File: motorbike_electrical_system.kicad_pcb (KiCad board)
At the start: 2 copper layers, 92.4 x 87.5 mm, 94 parts, among them IC1 BDX34C, IC2 BDX34C, IC3 BDX34C, IC4 BDX34C, IC5 BDX34C, IC6 BDX34C, U1 L7805, U2 L7805, U3 L7805

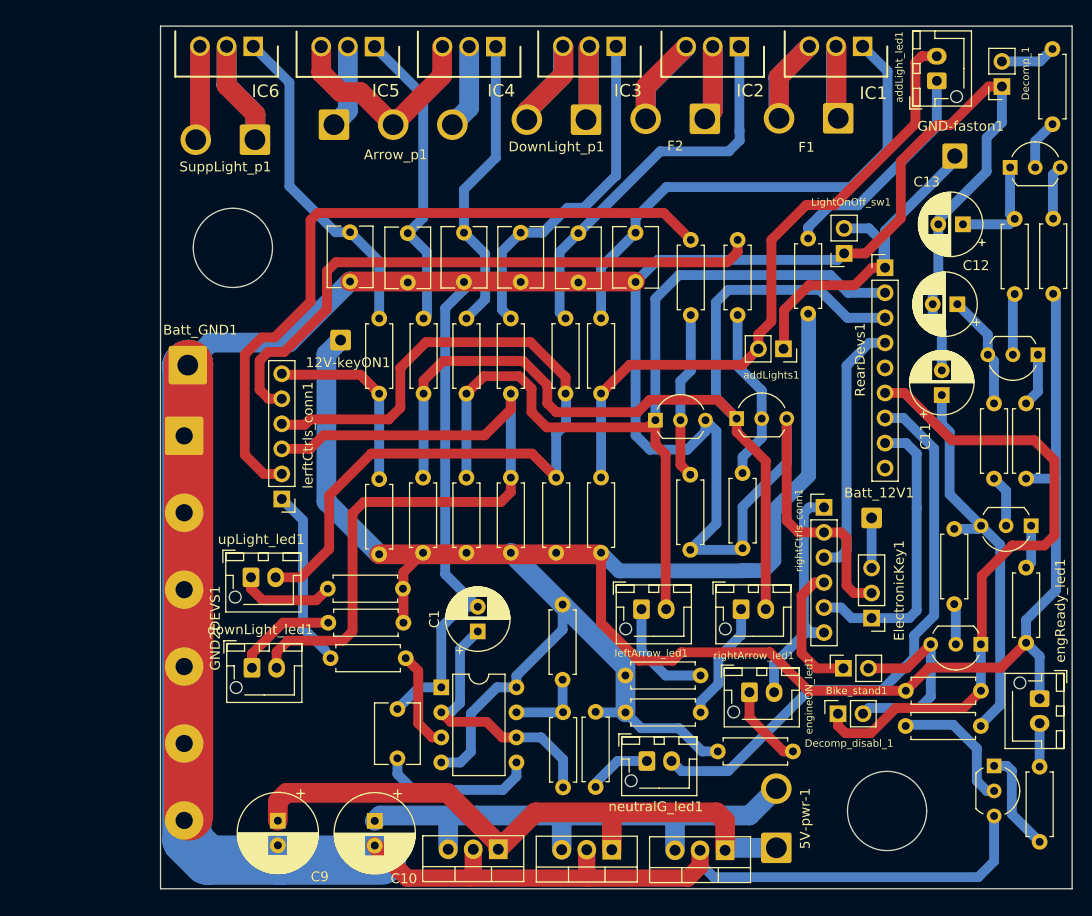
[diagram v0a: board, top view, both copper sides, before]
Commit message: PCB size reduction
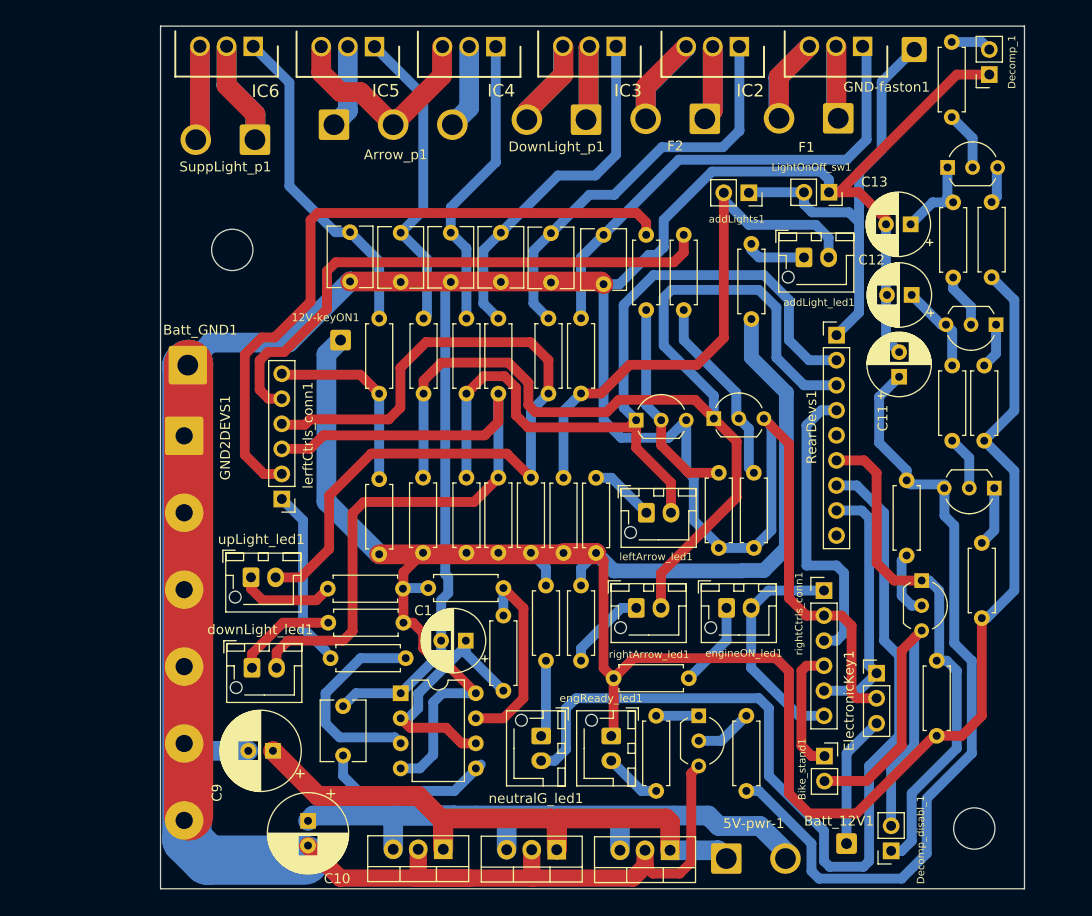
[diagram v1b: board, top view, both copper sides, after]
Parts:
- moved engReady_led1 43.6 mm to (168.9, 122.6)
- moved RA7 39.0 mm to (173.5, 128.2), turned to 90 degrees
- moved Batt_12V1 33.1 mm to (192.8, 133.5)
- moved DC5 30.4 mm to (177.8, 120.5)
- moved RL3 22.7 mm to (167.4, 96.4), turned to -90 degrees
- moved addLight_led1 22.4 mm to (188.5, 74.1), turned to 0 degrees
- moved addLights1 16.2 mm to (182.9, 67.5)
- moved RA5 16.2 mm to (182.6, 120.5), turned to -90 degrees
- moved Decomp_disabl_1 14.9 mm to (197.3, 134.2), turned to 180 degrees
- moved RL5 13.8 mm to (162.3, 115.0)
- moved RL4 13.2 mm to (165.9, 115.0), turned to 90 degrees
- moved RL6 12.9 mm to (176.8, 116.7)
- moved GND-faston1 11.6 mm to (199.7, 53.0)
- moved RC1 11.5 mm to (158.0, 110.4)
- moved RC2 11.1 mm to (158.0, 107.6), turned to 180 degrees
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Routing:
- net Net-(C11-Pad1): track 39.6 -> 81.6 mm
- net Net-(RearDevs1-Pad7): track 58.1 -> 94.6 mm
- net Net-(Bike_stand1-Pad2): track 20.2 -> 42.9 mm
- net GND: track 461.1 -> 440.4 mm
- net Net-(5V-pwr-1-Pad2): track 52.8 -> 72.7 mm
- net Net-(RL7-Pad1): track 23.1 -> 6.26 mm
- net Net-(DC4-Pad1): track 66.2 -> 52.6 mm
- net Net-(RC1-Pad1): track 8.05 -> 20.5 mm
- net Net-(RE1-Pad1): track 10.1 -> 21.4 mm
- net Net-(RBT6-Pad2): track 66.1 -> 55.8 mm
- net Net-(Batt_12V1-Pad1): track 5.08 -> 13.5 mm
- net Net-(Q_arr2-Pad1): track 99.0 -> 107.3 mm
- net Net-(GND-faston1-Pad1): track 37.4 -> 45.4 mm
- net Net-(DC5-Pad2): track 13.7 -> 5.88 mm
- net Net-(Q_arr1-Pad1): track 89.2 -> 82.4 mm
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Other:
- board size 92.4 x 87.5 mm -> 87.6 x 87.5 mm

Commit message: Fix: wrong power transistor orientation (and PCB's size reducing)
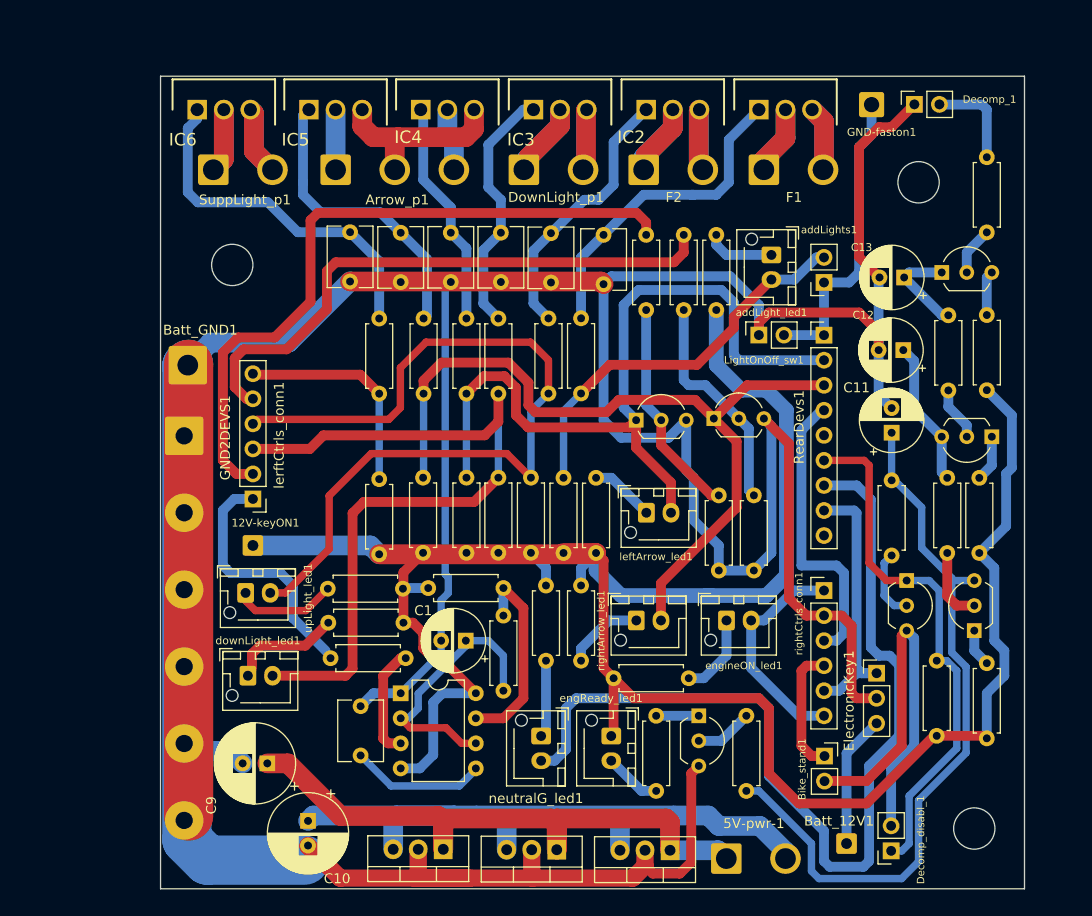
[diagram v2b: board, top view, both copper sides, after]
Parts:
- moved 12V-keyON1 22.6 mm to (132.6, 103.3)
- moved LightOnOff_sw1 16.1 mm to (183.9, 81.9), turned to 90 degrees
- moved DC3 14.6 mm to (205.7, 111.9), turned to 90 degrees
- moved IC1 12.3 mm to (183.9, 59.1), turned to 0 degrees
- moved RA8 12.2 mm to (207.0, 63.9)
- moved RL8 12.2 mm to (207.0, 115.2)
- moved addLights1 11.9 mm to (190.5, 76.6), turned to 180 degrees
- moved RA6 11.5 mm to (203.1, 79.9)
- moved RL10 11.5 mm to (207.0, 79.9)
- moved IC2 11.4 mm to (172.5, 59.1), turned to 0 degrees
- moved RA4 11.4 mm to (203.0, 96.4)
- moved RL9 11.4 mm to (206.3, 96.4)
- moved DC2 11.4 mm to (207.5, 92.2)
- moved DC1 10.7 mm to (202.4, 75.6)
- moved IC3 10.6 mm to (161.0, 59.1), turned to 0 degrees
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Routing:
- net Net-(Q_arr2-Pad1): track 107.3 -> 82.0 mm
- net +12V: track 264.2 -> 245.7 mm
- net Net-(C8-Pad1): track 49.7 -> 33.2 mm
- net Net-(RBT6-Pad2): track 55.8 -> 40.3 mm
- net Net-(C3-Pad1): track 42.0 -> 27.4 mm
- net Net-(GND-faston1-Pad1): track 45.4 -> 30.8 mm
- net Net-(C4-Pad1): track 36.0 -> 25.6 mm
- net Net-(RE1-Pad1): track 21.4 -> 11.4 mm
- net Net-(RE1-Pad2): track 17.2 -> 25.0 mm
- net Net-(C11-Pad1): track 81.6 -> 74.4 mm
- net Net-(IC6-Pad2): track 20.2 -> 13.1 mm
- net Net-(C5-Pad1): track 30.1 -> 23.1 mm
- net Net-(DownLight_p1-Pad2): track 17.9 -> 11.7 mm
- net Net-(Decomp_1-Pad2): track 4.13 -> 9.85 mm
- net Net-(F2-Pad2): track 18.0 -> 12.3 mm
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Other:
- board size 87.6 x 87.5 mm -> 87.6 x 82.4 mm

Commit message: enhancement: BDX34C replaced by D45VH10
In order to reduce the wasted electric power BDX34C (VCE=2.5V) has been replaced by D45VH10 (VCE=0.3V) for up-light and added-light
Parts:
- removed F1, F2, SuppLight_p1: Conn_01x02, Connector_Wire:SolderWire-1.5sqmm_1x02_P6mm_D1.7mm_OD3mm
- removed IC1, IC2: BDX34C, BDX34C:TO270P460X1020X2008-3P
- added Horn_p1: Conn_01x02, Connector_Wire:SolderWire-1.5sqmm_1x02_P6mm_D1.7mm_OD3mm, F.Cu at (127.1, 65.2)
- added Q1: D45VH10, Package_TO_SOT_THT:TO-220-3_Vertical, F.Cu at (187.0, 59.3)
- added Q2: D45VH10, Package_TO_SOT_THT:TO-220-3_Vertical, F.Cu at (175.3, 59.3)
- added UpLight_p1: Conn_01x02, Connector_Wire:SolderWire-1.5sqmm_1x02_P6mm_D1.7mm_OD3mm, F.Cu at (174.8, 65.2)
- added addLight_p1: Conn_01x02, Connector_Wire:SolderWire-1.5sqmm_1x02_P6mm_D1.7mm_OD3mm, F.Cu at (186.5, 64.9)
- BT5, RB1, RB2, RB3, RBT2, RBT3, RBT4, RC1, RC2: footprint Resistor_THT:R_Axial_DIN0207_L6.3mm_D2.5mm_P7.62mm_Horizontal -> Resistor_THT:R_Axial_DIN0204_L3.6mm_D1.6mm_P5.08mm_Horizontal
- RBT1, RBT6: footprint Resistor_THT:R_Axial_DIN0207_L6.3mm_D2.5mm_P7.62mm_Horizontal -> Resistor_THT:R_Axial_DIN0204_L3.6mm_D1.6mm_P7.62mm_Horizontal
- RTA1, RTA6: value 1.2K -> 100; footprint Resistor_THT:R_Axial_DIN0207_L6.3mm_D2.5mm_P7.62mm_Horizontal -> Resistor_THT:R_Axial_DIN0516_L15.5mm_D5.0mm_P20.32mm_Horizontal
- RTA2, RTA5: value 1.2K -> 2K
- RTA3, RTA4: value 1.2K -> 8K; footprint Resistor_THT:R_Axial_DIN0207_L6.3mm_D2.5mm_P7.62mm_Horizontal -> Resistor_THT:R_Axial_DIN0204_L3.6mm_D1.6mm_P7.62mm_Horizontal
- moved RTA6 13.2 mm to (166.6, 101.0)
- moved RC1 9.71 mm to (164.6, 117.5), turned to 180 degrees
- moved RBT6 9.48 mm to (162.8, 94.6)
- moved RBT1 9.38 mm to (160.5, 94.6)
- moved RL3 7.94 mm to (172.5, 102.5), turned to 0 degrees
- moved RBT3 7.59 mm to (148.6, 98.9)
- moved RBT2 7.54 mm to (151.9, 98.9)
- moved RB1 6.37 mm to (179.3, 99.5)
- moved RB2 6.37 mm to (182.9, 99.5)
- moved RTA1 6.11 mm to (156.5, 80.7)
- moved RTA3 5.65 mm to (148.6, 80.2)
- moved RTA2 5.59 mm to (151.9, 80.2)
- moved RBT4 5.43 mm to (145.0, 93.9)
- moved RTA4 4.86 mm to (145.0, 80.2)
- moved Decomp_1 4.81 mm to (204.5, 58.5)
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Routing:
- net Net-(RBT1-Pad2): track 85.6 -> 107.8 mm
- net Net-(Q2-Pad2): track 0.00 -> 14.2 mm
- net Net-(F2-Pad1): track 14.2 -> 0.00 mm
- net Net-(F1-Pad1): track 14.0 -> 0.00 mm
- net Net-(Q1-Pad2): track 0.00 -> 13.9 mm
- net Net-(F1-Pad2): track 13.3 -> 0.00 mm
- net Net-(F2-Pad2): track 12.3 -> 0.00 mm
- net Net-(Q2-Pad3): track 0.00 -> 12.1 mm
- net Net-(Q1-Pad3): track 0.00 -> 11.8 mm
- net Net-(RBT2-Pad2): track 77.9 -> 67.4 mm
- net Net-(RBT6-Pad2): track 40.3 -> 49.2 mm
- net Net-(GND-faston1-Pad1): track 30.8 -> 39.7 mm
- net Net-(C8-Pad1): track 33.2 -> 40.4 mm
- net Net-(BT5-Pad1): track 22.3 -> 16.0 mm
- net Net-(C3-Pad1): track 27.4 -> 33.4 mm
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
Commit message: First release of all-in-one solution
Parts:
- removed 12V-keyON1, Batt_12V1: Conn_01x01, Connector_Wire:SolderWire-0.5sqmm_1x01_D0.9mm_OD2.1mm
- removed 5V-pwr-1: Conn_01x02, Connector_Wire:SolderWire-1.5sqmm_1x02_P6mm_D1.7mm_OD3mm
- removed BT5, RB1, RB2, RB3, RBT2, RBT3, RBT4, RC1, RC2: 100K, Resistor_THT:R_Axial_DIN0204_L3.6mm_D1.6mm_P5.08mm_Horizontal
- removed Batt_GND1: Conn_01x01, Connector_Wire:SolderWire-1.5sqmm_1x01_D1.7mm_OD3.9mm
- removed C1: 1uF, Capacitor_THT:CP_Radial_D6.3mm_P2.50mm
- removed C10: C_Polarized_Small, Capacitor_THT:CP_Radial_D8.0mm_P2.50mm
- removed C11, C12, C13: 50uF, Capacitor_THT:CP_Radial_D6.3mm_P2.50mm
- removed C2, C3, C4, C5, C6, C7, C8: 100nf, Capacitor_THT:C_Disc_D6.0mm_W4.4mm_P5.00mm
- removed DC1: BC327, Package_TO_SOT_THT:TO-92_Inline_Wide
- removed DC2, DC3, DC4, DC5, Q_arr1, Q_arr2: BC337, Package_TO_SOT_THT:TO-92_Inline_Wide
- removed Decomp_disabl_1: Conn_01x02, Connector_PinSocket_2.54mm:PinSocket_1x02_P2.54mm_Vertical
- removed ElectronicKey1: Conn_01x03, Connector_PinHeader_2.54mm:PinHeader_1x03_P2.54mm_Vertical
- removed GND-faston1: Conn_01x01, Connector_Wire:SolderWire-0.75sqmm_1x01_D1.25mm_OD2.3mm
- removed GND2DEVS1: Conn_01x06, Connector_Wire:SolderWire-1sqmm_1x06_P7.8mm_D1.4mm_OD3.9mm
- removed IC4, IC5, IC6: BDX34C, BDX34C:TO270P460X1020X2008-3P
- removed RBT1, RBT6: 100K, Resistor_THT:R_Axial_DIN0204_L3.6mm_D1.6mm_P7.62mm_Horizontal
- removed RE1: 5K, Resistor_THT:R_Axial_DIN0207_L6.3mm_D2.5mm_P7.62mm_Horizontal
- removed RL1, RL10, RL2, RL3, RL4, RL5, RL6, RL7, RL8, RL9: 1.2K, Resistor_THT:R_Axial_DIN0207_L6.3mm_D2.5mm_P7.62mm_Horizontal
- removed RTA1, RTA6: 100, Resistor_THT:R_Axial_DIN0516_L15.5mm_D5.0mm_P20.32mm_Horizontal
- removed RTA2, RTA5: 2K, Resistor_THT:R_Axial_DIN0207_L6.3mm_D2.5mm_P7.62mm_Horizontal
- removed RTA3, RTA4: 8K, Resistor_THT:R_Axial_DIN0204_L3.6mm_D1.6mm_P7.62mm_Horizontal
- removed addLight_led1, downLight_led1, engReady_led1, engineON_led1, leftArrow_led1, neutralG_led1, rightArrow_led1, upLight_led1: Conn_01x02, Connector_JST:JST_XH_B2B-XH-AM_1x02_P2.50mm_Vertical
- removed lerftCtrls_conn1: Conn_01x06, Connector_PinHeader_2.54mm:PinHeader_1x06_P2.54mm_Vertical
- removed sqWaveGen1: NE555P, Package_DIP:DIP-8_W7.62mm
- added Battery1: Conn_01x02, Connector_Wire:SolderWire-0.75sqmm_1x02_P7mm_D1.25mm_OD3.5mm, F.Cu at (170.9, 135.8)
- added D1: DIODE, Diode_THT:D_DO-34_SOD68_P7.62mm_Horizontal, F.Cu at (135.4, 116.2)
- added D2: DIODE, Diode_THT:D_DO-34_SOD68_P7.62mm_Horizontal, F.Cu at (137.9, 116.2)
- added IC2: BDX34C, BDX34C:TO270P460X1020X2008-3P, F.Cu at (183.0, 59.1)
- added K1: RT42xxxx, Relay_THT:Relay_DPDT_Schrack-RT2-FormC_RM5mm, F.Cu at (207.3, 106.6)
- added KeyLocker1: Conn_01x08, Connector_PinHeader_2.54mm:PinHeader_1x08_P2.54mm_Vertical, F.Cu at (205.2, 76.8)
- added LEDs_conn1: Conn_01x08, Connector_PinHeader_2.54mm:PinHeader_1x08_P2.54mm_Vertical, F.Cu at (116.3, 115.0)
- added Q10: BC337, Package_TO_SOT_THT:TO-92L_Inline_Wide, F.Cu at (144.0, 85.9)
- added Q11: BC337, Package_TO_SOT_THT:TO-92L_Inline_Wide, F.Cu at (144.0, 123.8)
- added Q12: BC327, Package_TO_SOT_THT:TO-92L_Inline_Wide, F.Cu at (126.3, 124.1)
- added Q13: BC337, Package_TO_SOT_THT:TO-92L_Inline_Wide, F.Cu at (160.0, 124.6)
- added Q14: D45VH10, Package_TO_SOT_THT:TO-220-3_Vertical, F.Cu at (156.5, 59.3)
- added Q15: D45VH10, Package_TO_SOT_THT:TO-220-3_Vertical, F.Cu at (196.3, 59.3)
- added Q3: BC337, Package_TO_SOT_THT:TO-92L_Inline_Wide, F.Cu at (144.0, 114.2)
- added Q4: BC337, Package_TO_SOT_THT:TO-92L_Inline_Wide, F.Cu at (144.0, 109.4)
- added Q5: BC337, Package_TO_SOT_THT:TO-92L_Inline_Wide, F.Cu at (144.0, 104.5)
- added Q6: BC337, Package_TO_SOT_THT:TO-92L_Inline_Wide, F.Cu at (144.0, 99.9)
- added Q7: BC337, Package_TO_SOT_THT:TO-92L_Inline_Wide, F.Cu at (144.0, 95.2)
- added Q8: BC337, Package_TO_SOT_THT:TO-92L_Inline_Wide, F.Cu at (144.0, 90.6)
- added Q9: BC337, Package_TO_SOT_THT:TO-92L_Inline_Wide, F.Cu at (144.0, 119.0)
- added R1: 500, Resistor_THT:R_Axial_DIN0309_L9.0mm_D3.2mm_P12.70mm_Horizontal, F.Cu at (191.8, 72.5)
- added RA10: 240, Resistor_THT:R_Axial_DIN0414_L11.9mm_D4.5mm_P15.24mm_Horizontal, F.Cu at (128.8, 89.0)
- added RA11: 240, Resistor_THT:R_Axial_DIN0414_L11.9mm_D4.5mm_P15.24mm_Horizontal, F.Cu at (133.9, 89.0)
- added RA12: 240, Resistor_THT:R_Axial_DIN0414_L11.9mm_D4.5mm_P15.24mm_Horizontal, F.Cu at (138.9, 89.0)
- added RA13: 8K, Resistor_THT:R_Axial_DIN0207_L6.3mm_D2.5mm_P7.62mm_Horizontal, F.Cu at (145.6, 81.2)
- added RA14: 8K, Resistor_THT:R_Axial_DIN0207_L6.3mm_D2.5mm_P7.62mm_Horizontal, F.Cu at (148.6, 81.2)
- added RA15: 240, Resistor_THT:R_Axial_DIN0207_L6.3mm_D2.5mm_P7.62mm_Horizontal, F.Cu at (138.2, 119.3)
- added RA16: 5K, Resistor_THT:R_Axial_DIN0207_L6.3mm_D2.5mm_P7.62mm_Horizontal, F.Cu at (154.7, 93.9)
- added RA17: 5K, Resistor_THT:R_Axial_DIN0207_L6.3mm_D2.5mm_P7.62mm_Horizontal, F.Cu at (154.7, 96.9)
- added RA18: 5K, Resistor_THT:R_Axial_DIN0207_L6.3mm_D2.5mm_P7.62mm_Horizontal, F.Cu at (154.7, 101.2)
- added RA19: 5K, Resistor_THT:R_Axial_DIN0207_L6.3mm_D2.5mm_P7.62mm_Horizontal, F.Cu at (154.7, 104.3)
- added RA20: 5K, Resistor_THT:R_Axial_DIN0207_L6.3mm_D2.5mm_P7.62mm_Horizontal, F.Cu at (154.7, 107.3)
- added RA21: 5K, Resistor_THT:R_Axial_DIN0207_L6.3mm_D2.5mm_P7.62mm_Horizontal, F.Cu at (154.7, 110.4)
- added RA22: 5K, Resistor_THT:R_Axial_DIN0207_L6.3mm_D2.5mm_P7.62mm_Horizontal, F.Cu at (154.7, 113.4)
- added RA23: 5K, Resistor_THT:R_Axial_DIN0207_L6.3mm_D2.5mm_P7.62mm_Horizontal, F.Cu at (154.7, 116.5)
- added RA24: 100K, Resistor_THT:R_Axial_DIN0207_L6.3mm_D2.5mm_P7.62mm_Horizontal, F.Cu at (130.6, 128.7)
- added RA25: 100K, Resistor_THT:R_Axial_DIN0207_L6.3mm_D2.5mm_P7.62mm_Horizontal, F.Cu at (119.9, 118.3)
- added RA26: 100K, Resistor_THT:R_Axial_DIN0207_L6.3mm_D2.5mm_P7.62mm_Horizontal, F.Cu at (119.9, 121.3)
- added RA27: 100K, Resistor_THT:R_Axial_DIN0207_L6.3mm_D2.5mm_P7.62mm_Horizontal, F.Cu at (150.4, 127.4)
- added RA28: 100K, Resistor_THT:R_Axial_DIN0207_L6.3mm_D2.5mm_P7.62mm_Horizontal, F.Cu at (130.6, 125.6)
- added RA9: 0, Resistor_THT:R_Axial_DIN0207_L6.3mm_D2.5mm_P10.16mm_Horizontal, F.Cu at (130.1, 96.9)
- added U4: ATmega16L-8P, Package_DIP:DIP-40_W15.24mm, F.Cu at (167.1, 73.6)
- added leftCtrls-faston1: Conn_01x01, Connector_Wire:SolderWire-0.75sqmm_1x01_D1.25mm_OD2.3mm, F.Cu at (191.8, 129.4)
- added leftCtrls_conn1: Conn_01x06, Connector_PinHeader_2.54mm:PinHeader_1x06_P2.54mm_Vertical, F.Cu at (122.2, 74.3)
- RA1, RA2: value 5K -> 0; footprint Resistor_THT:R_Axial_DIN0207_L6.3mm_D2.5mm_P7.62mm_Horizontal -> Resistor_THT:R_Axial_DIN0207_L6.3mm_D2.5mm_P10.16mm_Horizontal
- RA3, RA5: value 12K -> 0; footprint Resistor_THT:R_Axial_DIN0207_L6.3mm_D2.5mm_P7.62mm_Horizontal -> Resistor_THT:R_Axial_DIN0207_L6.3mm_D2.5mm_P10.16mm_Horizontal
- RA4, RA6: value 24K -> 0; footprint Resistor_THT:R_Axial_DIN0207_L6.3mm_D2.5mm_P7.62mm_Horizontal -> Resistor_THT:R_Axial_DIN0207_L6.3mm_D2.5mm_P10.16mm_Horizontal
- RA7: value 1.2K -> 1K
- RA8: value 24K -> 3K
- moved Bike_stand1 80.7 mm to (116.9, 91.8), turned to 90 degrees
- moved RA8 76.6 mm to (154.7, 119.8), turned to 0 degrees
- moved RA6 75.8 mm to (130.1, 100.0), turned to 180 degrees
- moved RA4 73.6 mm to (130.1, 106.1), turned to 180 degrees
- moved RA3 68.5 mm to (130.1, 109.1), turned to 180 degrees
- moved Horn_p1 67.3 mm to (194.4, 65.9)
- moved RA2 56.7 mm to (130.1, 112.2), turned to 180 degrees
- moved Q1 56.4 mm to (130.6, 59.3)
- moved RA1 55.9 mm to (130.1, 115.2), turned to 180 degrees
- moved RearDevs1 55.8 mm to (175.8, 135.8), turned to 90 degrees
- moved RA5 55.4 mm to (130.1, 103.0), turned to 180 degrees
- moved addLight_p1 55.1 mm to (131.4, 66.2)
- moved Decomp_1 52.4 mm to (189.1, 108.7)
- moved RA7 35.8 mm to (138.2, 122.3), turned to 180 degrees
- moved Arrow_p1 32.3 mm to (173.2, 66.2)
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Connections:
- net Net-(5V-pwr-1-Pad2) renamed +5V
- net Net-(ElectronicKey1-Pad1) renamed c_engineOFF
- Bike_stand1 pad 1: Net-(Bike_stand1-Pad1) -> GND
- Bike_stand1 pad 2: Net-(Bike_stand1-Pad2) -> i_bykeStand
- C9 pad 1: Net-(5V-pwr-1-Pad1) -> +12V
- Decomp_1 pad 1: GND -> i_decompr
- Decomp_1 pad 2: Net-(Decomp_1-Pad2) -> GND
- IC3 pad 2: Net-(DownLight_p1-Pad1) -> Net-(Arrow_p1-Pad1)
- IC3 pad 3: Net-(DownLight_p1-Pad2) -> Net-(Arrow_p1-Pad2)
- LightOnOff_sw1 pad 2: Net-(GND-faston1-Pad1) -> i_lightON/OFF
- RA3 pad 1: Net-(C11-Pad1) -> Net-(D1-Pad2)
- RA4 pad 1: Net-(C12-Pad1) -> c_leftArrow
- RA5 pad 2: Net-(C11-Pad1) -> Net-(LEDs_conn1-Pad5)
- RA8 pad 1: Net-(Decomp_1-Pad2) -> Net-(Q11-Pad2)
- RA8 pad 2: Net-(DC1-Pad2) -> o_keepAlive
- RearDevs1 pad 1: Net-(GND-faston1-Pad1) -> c_rearLight
- RearDevs1 pad 2: Net-(Q_arr1-Pad1) -> c_leftArrow
- RearDevs1 pad 3: Net-(Q_arr2-Pad1) -> c_rightArrow
- RearDevs1 pad 4: Net-(RearDevs1-Pad4) -> o_stopLight
- RearDevs1 pad 5: unconnected-(RearDevs1-Pad5) -> i_brakeSwitch
- RearDevs1 pad 6: Net-(DC4-Pad1) -> o_startEngine
- RearDevs1 pad 7: Net-(RearDevs1-Pad7) -> i_neutral
- U1 pad 1: Net-(5V-pwr-1-Pad1) -> +12V
- U2 pad 1: Net-(5V-pwr-1-Pad1) -> +12V
- U3 pad 1: Net-(5V-pwr-1-Pad1) -> +12V
- addLights1 pad 1: Net-(GND-faston1-Pad1) -> GND
- addLights1 pad 2: Net-(RBT6-Pad2) -> i_addLight
- rightCtrls_conn1 pad 1: Net-(engineON_led1-Pad2) -> GND
- rightCtrls_conn1 pad 3: Net-(RearDevs1-Pad4) -> i_brakeSwitch
- rightCtrls_conn1 pad 4: Net-(Bike_stand1-Pad1) -> i_startButton
- rightCtrls_conn1 pad 6: Net-(engineON_led1-Pad2) -> i_engineON
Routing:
- net GND: track 439.9 -> 259.5 mm
- net Net-(Q15-Pad1): track 0.00 -> 144.4 mm, vias 0 -> 2
- net tempPower: track 0.00 -> 139.0 mm
- net c_leftArrow: track 0.00 -> 131.2 mm
- net +5V: track 74.2 -> 198.0 mm
- net Net-(RBT1-Pad2): track 107.8 -> 0.00 mm
- net Net-(RearDevs1-Pad7): track 96.5 -> 0.00 mm
- net Net-(Q7-Pad1): track 5.88 -> 93.0 mm
- net Net-(Q_arr2-Pad1): track 84.4 -> 0.00 mm
- net Net-(Q_arr1-Pad1): track 81.0 -> 0.00 mm
- net Net-(K1-PadA1): track 0.00 -> 78.6 mm, vias 0 -> 1
- net Net-(C11-Pad1): track 74.4 -> 0.00 mm
- net Net-(D1-Pad2): track 0.00 -> 69.3 mm
- net i_neutral: track 0.00 -> 68.3 mm
- net Net-(RBT2-Pad2): track 67.4 -> 0.00 mm
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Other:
- board size 87.6 x 82.4 mm -> 101.9 x 82.9 mm

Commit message: fix: duplicated signal
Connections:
- U4 pad 34: i_brakeSwitch -> unconnected-(U4-Pad34)
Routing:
- net i_brakeSwitch: track 63.4 -> 29.8 mm, vias 2 -> 0
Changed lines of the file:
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@@
   (net 92 "Net-(Q15-Pad1)")
   (net 93 "Net-(Q2-Pad2)")
+  (net 94 "unconnected-(U4-Pad34)")
   (footprint "Connector_PinSocket_2.54mm:PinSocket_1x02_P2.54mm_Vertical" (layer "F.Cu")
     (at 191.631 101.615 -90)
@@
       (net 69 "i_neutral") (pinfunction "PA7") (pintype "bidirectional"))
     (pad "34" thru_hole oval (at 15.24 15.24) (size 1.6 1.6) (drill 0.8) (layers *.Cu *.Mask)
-      (net 50 "i_brakeSwitch") (pinfunction "PA6") (pintype "bidirectional"))
+      (net 94 "unconnected-(U4-Pad34)") (pinfunction "PA6") (pintype "bidirectional"))
     (pad "35" thru_hole oval (at 15.24 12.7) (size 1.6 1.6) (drill 0.8) (layers *.Cu *.Mask)
       (net 70 "unconnected-(U4-Pad35)") (pinfunction "PA5") (pintype "bidirectional+no_connect"))
@@
   (segment (start 183.513 117.871) (end 182.375 116.733) (width 0.7) (layer "B.Cu") (net 49))
   (segment (start 191.778 117.871) (end 183.513 117.871) (width 0.7) (layer "B.Cu") (net 49))
-  (segment (start 182.375 119.273) (end 178.57 115.468) (width 0.7) (layer "F.Cu") (net 50))
-  (segment (start 178.57 115.468) (end 178.57 101.234) (width 0.7) (layer "F.Cu") (net 50))
-  (segment (start 182.375 88.793) (end 178.57 92.598) (width 0.75) (layer "F.Cu") (net 50))
-  (segment (start 178.57 92.598) (end 178.57 96.916) (width 0.75) (layer "F.Cu") (net 50))
-  (via (at 178.57 101.234) (size 0.8) (drill 0.4) (layers "F.Cu" "B.Cu") (net 50))
-  (via (at 178.57 96.916) (size 0.8) (drill 0.4) (layers "F.Cu" "B.Cu") (net 50))
   (segment (start 191.778 120.411) (end 183.513 120.411) (width 0.7) (layer "B.Cu") (net 50))
   (segment (start 183.513 120.411) (end 182.375 119.273) (width 0.7) (layer "B.Cu") (net 50))
@@
   (segment (start 180.602 130.434) (end 180.602 120.284) (width 1) (layer "B.Cu") (net 50))
   (segment (start 180.602 120.284) (end 181.613 119.273) (width 1) (layer "B.Cu") (net 50))
-  (segment (start 178.57 96.916) (end 178.57 101.234) (width 0.75) (layer "B.Cu") (net 50))
   (segment (start 191.778 112.791) (end 183.777 112.791) (width 0.7) (layer "B.Cu") (net 51))
   (segment (start 183.777 112.791) (end 182.375 114.193) (width 0.7) (layer "B.Cu") (net 51))
